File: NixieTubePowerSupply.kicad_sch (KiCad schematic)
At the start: 33 parts, among them J1 Barrel_Jack_Switch, J10 Conn_01x02_Pin, J11 Screw_Terminal_01x02, J2 Conn_01x02_Pin, J3 Screw_Terminal_01x02, J4 Conn_01x03_Pin, J5 Conn_01x03_Pin, J6 Screw_Terminal_01x03, J7 Conn_01x02_Pin, J8 Conn_01x02_Pin, J9 Conn_01x02_Pin, Q1 2SA1015, Q2 TK10A60D, U1 NJM7805, U2 NJM2360AD

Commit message: 配置を完了
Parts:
- removed J11: Screw_Terminal_01x02, mylib:TerminalBlock_TB111-2-2_P5.08mm, symbol Connector:Screw_Terminal_01x02
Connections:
- net 200V: now also J6.3 (Pin_3); no longer J6.1 (Pin_1)
- net GND: now also J6.1 (Pin_1); no longer J6.3 (Pin_3)

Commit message: 配線を完了
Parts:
- U2: footprint Package_DIP:DIP-8_W7.62mm -> Package_DIP:DIP-8_W7.62mm_Socket
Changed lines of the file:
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@@
       (effects (font (size 1.27 1.27)))
     )
-    (property "Footprint" "Package_DIP:DIP-8_W7.62mm" (at 100.33 82.55 0)
+    (property "Footprint" "Package_DIP:DIP-8_W7.62mm_Socket" (at 100.33 82.55 0)
       (effects (font (size 1.27 1.27)) hide)
     )

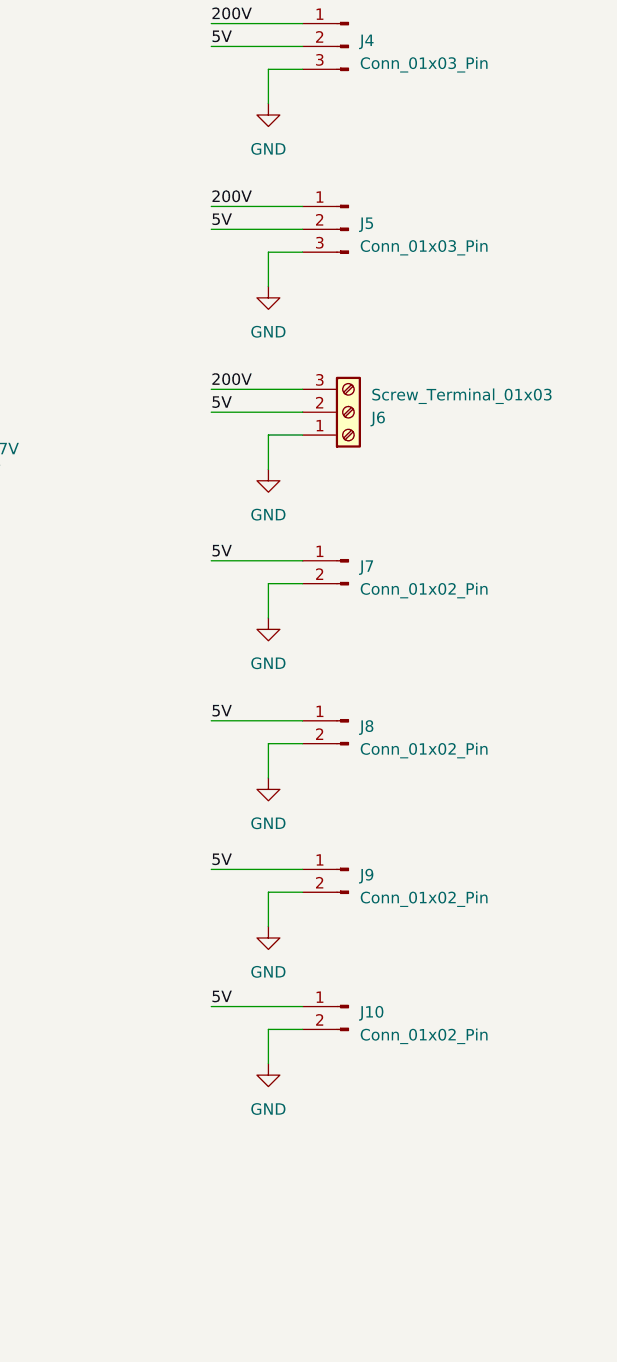
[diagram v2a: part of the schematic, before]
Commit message: 基板サイズを共有のものに変更
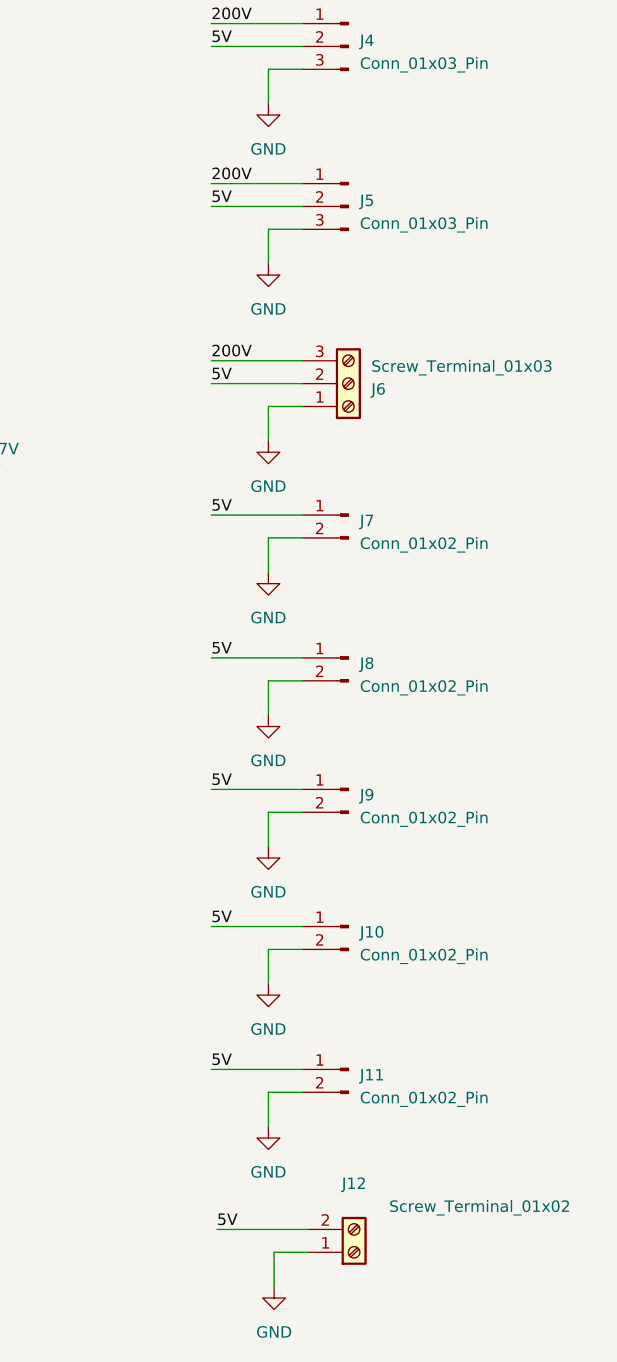
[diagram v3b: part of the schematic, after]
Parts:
- added J11: Conn_01x02_Pin, Connector_JST:JST_XH_B2B-XH-A_1x02_P2.50mm_Vertical, symbol Connector:Conn_01x02_Pin
- added J12: Screw_Terminal_01x02, mylib:TerminalBlock_TB111-2-2_P5.08mm, symbol Connector:Screw_Terminal_01x02
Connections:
- net 5V: now also J11.1 (Pin_1), J12.2 (Pin_2)
- net GND: now also J11.2 (Pin_2), J12.1 (Pin_1)
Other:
- moved on the sheet: J10, J5, J6, J7, J8, J9

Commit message: 製造後データを追加
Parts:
- added D1: ON, LED_THT:LED_D3.0mm, symbol Device:LED
- added R1: 10k, Resistor_THT:R_Axial_DIN0207_L6.3mm_D2.5mm_P10.16mm_Horizontal, symbol Device:R
- added SW1: SW_SPDT, mylib:Switch_Toggle_2MS1-T1-B4-M2-Q-E, symbol Switch:SW_SPDT
- D2: renamed from D1; value 1N4148 -> 4148
- renumbered D2 to D3, R1 to R2, R2 to R3, R3 to R4, R4 to R5, R5 to R6, R6 to R7
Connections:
- net 12V: now also SW1.2 (B); no longer C1.1, C2.1, C4.1, C5.1, R2.1, U1.1 (IN), U2.6 (V+)
- net GND: now also R1.2
- net at R7.1, U2.5 (INV): now also RV1.1; no longer RV1.3
- net at R6.2, RV1.2: now also RV1.3; no longer RV1.1
- new net: C1.1, C2.1, C4.1, C5.1, D1.2 (A), R2.1, SW1.1 (A), U1.1 (IN), U2.6 (V+)
- new net: D1.1 (K), R1.1
- no-connect marks 0 -> 1
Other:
- moved on the sheet: C1, C2, C3, C4, C5, C6, C7, C8, D2, D3, J1, J2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
